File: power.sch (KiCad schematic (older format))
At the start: 157 parts, among them J1 Conn_BAT, Q1 BSS138, Q2 BSS138, Q3 BSS138, Q4 BSS138, Q5 BSS138, SW1 SW_WAKEUP, SW2 SW_RESET, U1 SAMA5D2x-SIP, U3 ACT8945A

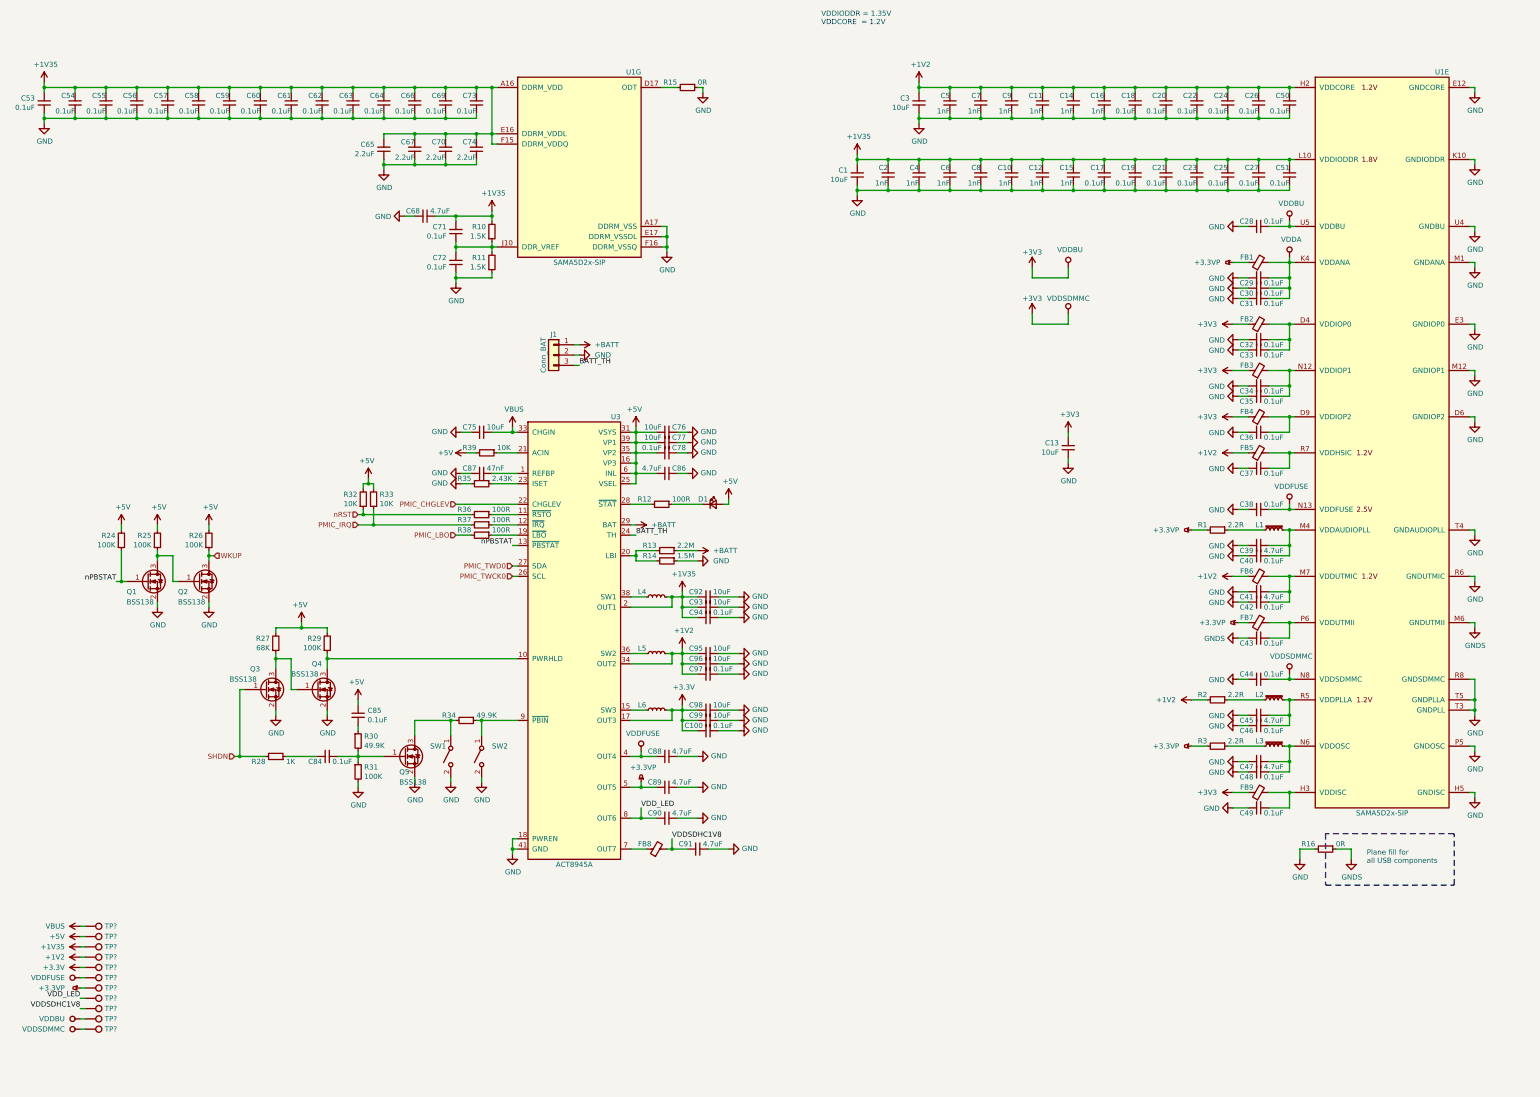
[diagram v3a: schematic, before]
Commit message: Finish schematic (?), set footprints and start placement
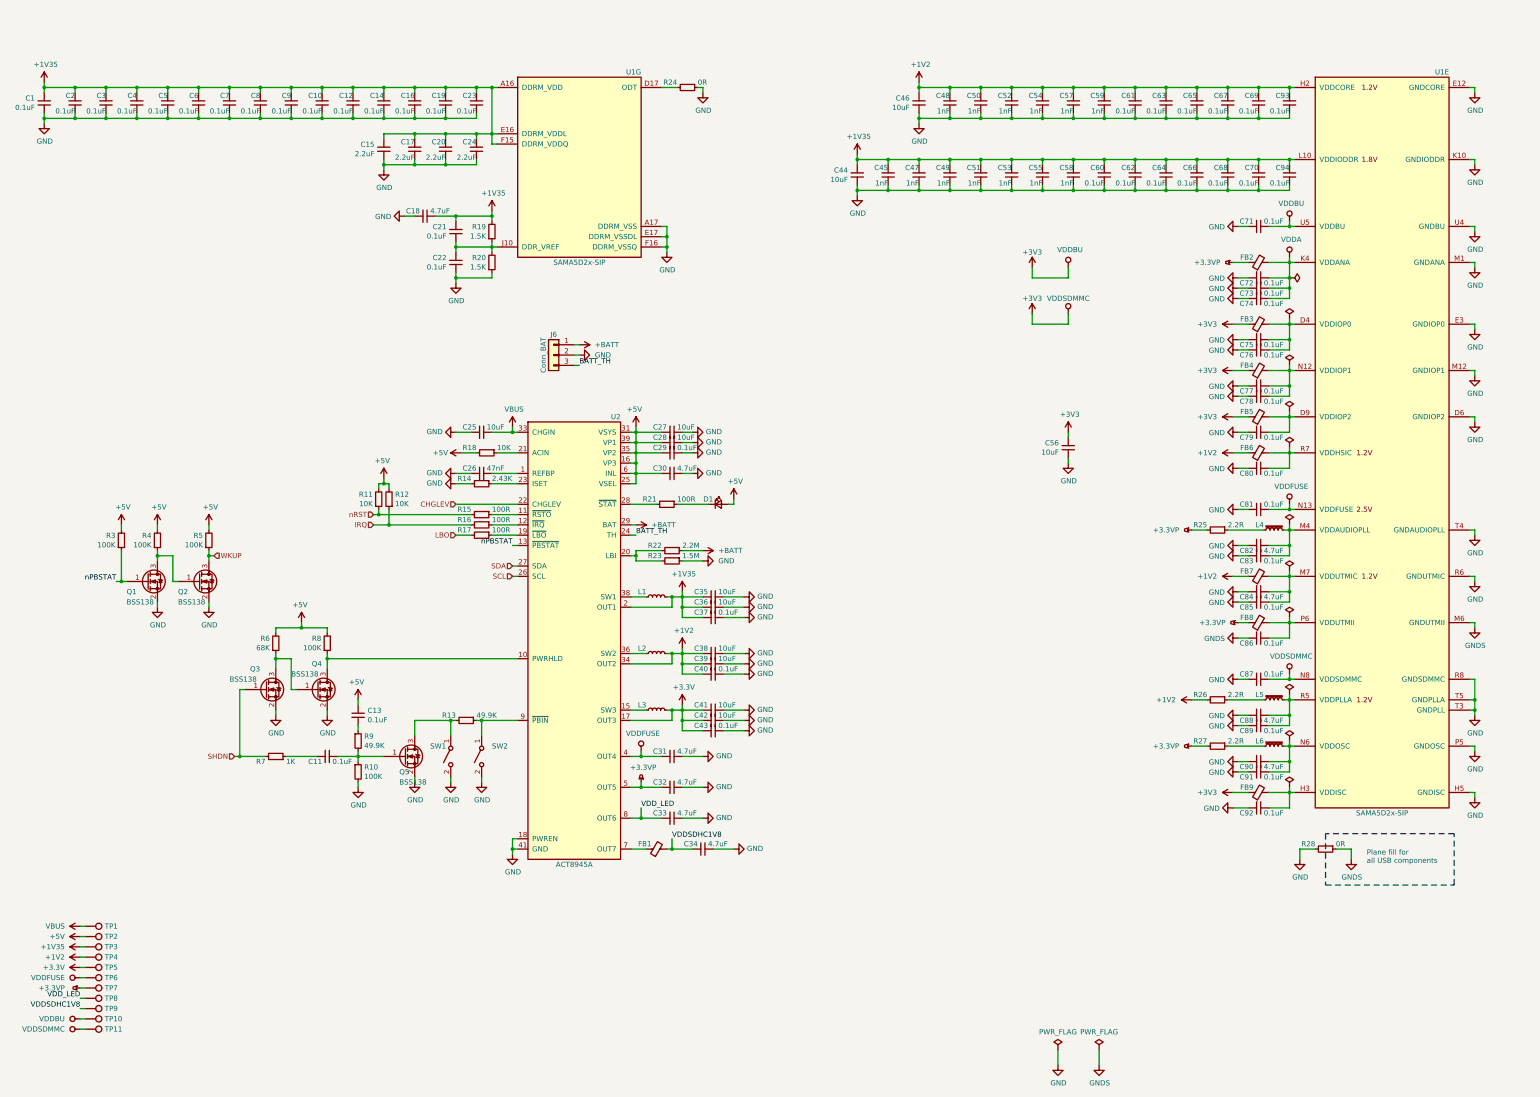
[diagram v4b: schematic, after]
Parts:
- C1: renamed from C53; footprint Capacitor_SMD:C_0603_1608Metric -> Capacitor_SMD:C_0402_1005Metric
- C10: renamed from C62; footprint Capacitor_SMD:C_0603_1608Metric -> Capacitor_SMD:C_0402_1005Metric
- C11: renamed from C84; footprint Capacitor_SMD:C_0603_1608Metric -> Capacitor_SMD:C_0402_1005Metric
- C12: renamed from C63; footprint Capacitor_SMD:C_0603_1608Metric -> Capacitor_SMD:C_0402_1005Metric
- C13: renamed from C85; footprint (none) -> Capacitor_SMD:C_0402_1005Metric
- C14: renamed from C64; footprint Capacitor_SMD:C_0603_1608Metric -> Capacitor_SMD:C_0402_1005Metric
- C15: renamed from C65; footprint Capacitor_SMD:C_0603_1608Metric -> Capacitor_SMD:C_0402_1005Metric
- C16: renamed from C66; footprint Capacitor_SMD:C_0603_1608Metric -> Capacitor_SMD:C_0402_1005Metric
- C17: renamed from C67; footprint Capacitor_SMD:C_0603_1608Metric -> Capacitor_SMD:C_0402_1005Metric
- C18: renamed from C68; footprint Capacitor_SMD:C_0603_1608Metric -> Capacitor_SMD:C_0402_1005Metric
- C19: renamed from C69; footprint Capacitor_SMD:C_0603_1608Metric -> Capacitor_SMD:C_0402_1005Metric
- C2: renamed from C54; footprint Capacitor_SMD:C_0603_1608Metric -> Capacitor_SMD:C_0402_1005Metric
- C20: renamed from C70; footprint Capacitor_SMD:C_0603_1608Metric -> Capacitor_SMD:C_0402_1005Metric
- C21: renamed from C71; footprint (none) -> Capacitor_SMD:C_0402_1005Metric
- C22: renamed from C72; footprint (none) -> Capacitor_SMD:C_0402_1005Metric
- C23: renamed from C73; footprint Capacitor_SMD:C_0603_1608Metric -> Capacitor_SMD:C_0402_1005Metric
- C24: renamed from C74; footprint Capacitor_SMD:C_0603_1608Metric -> Capacitor_SMD:C_0402_1005Metric
- C25: renamed from C75; footprint Capacitor_SMD:C_0603_1608Metric -> Capacitor_SMD:C_0402_1005Metric
- C26: renamed from C87; footprint Capacitor_SMD:C_0603_1608Metric -> Capacitor_SMD:C_0402_1005Metric
- C27: renamed from C76; footprint Capacitor_SMD:C_0603_1608Metric -> Capacitor_SMD:C_0402_1005Metric
- C28: renamed from C77; footprint Capacitor_SMD:C_0603_1608Metric -> Capacitor_SMD:C_0402_1005Metric
- C29: renamed from C78; footprint Capacitor_SMD:C_0603_1608Metric -> Capacitor_SMD:C_0402_1005Metric
- C3: renamed from C55; footprint Capacitor_SMD:C_0603_1608Metric -> Capacitor_SMD:C_0402_1005Metric
- C30: renamed from C86; footprint Capacitor_SMD:C_0603_1608Metric -> Capacitor_SMD:C_0402_1005Metric
- C31: renamed from C88; footprint Capacitor_SMD:C_0603_1608Metric -> Capacitor_SMD:C_0402_1005Metric
- C32: renamed from C89; footprint Capacitor_SMD:C_0603_1608Metric -> Capacitor_SMD:C_0402_1005Metric
- C33: renamed from C90; footprint Capacitor_SMD:C_0603_1608Metric -> Capacitor_SMD:C_0402_1005Metric
- C34: renamed from C91; footprint Capacitor_SMD:C_0603_1608Metric -> Capacitor_SMD:C_0402_1005Metric
- C35: renamed from C92; footprint Capacitor_SMD:C_0603_1608Metric -> Capacitor_SMD:C_0402_1005Metric
- C36: renamed from C93; footprint Capacitor_SMD:C_0603_1608Metric -> Capacitor_SMD:C_0402_1005Metric
- C37: renamed from C94; footprint Capacitor_SMD:C_0603_1608Metric -> Capacitor_SMD:C_0402_1005Metric
- C38: renamed from C95; footprint Capacitor_SMD:C_0603_1608Metric -> Capacitor_SMD:C_0402_1005Metric
- C39: renamed from C96; footprint Capacitor_SMD:C_0603_1608Metric -> Capacitor_SMD:C_0402_1005Metric
- C4: renamed from C56; footprint Capacitor_SMD:C_0603_1608Metric -> Capacitor_SMD:C_0402_1005Metric
- C40: renamed from C97; footprint Capacitor_SMD:C_0603_1608Metric -> Capacitor_SMD:C_0402_1005Metric
- C41: renamed from C98; footprint Capacitor_SMD:C_0603_1608Metric -> Capacitor_SMD:C_0402_1005Metric
- C42: renamed from C99; footprint Capacitor_SMD:C_0603_1608Metric -> Capacitor_SMD:C_0402_1005Metric
- C43: renamed from C100; footprint Capacitor_SMD:C_0603_1608Metric -> Capacitor_SMD:C_0402_1005Metric
- C44: renamed from C1; footprint Capacitor_SMD:C_0603_1608Metric -> Capacitor_SMD:C_0402_1005Metric
- C45: renamed from C2; footprint Capacitor_SMD:C_0603_1608Metric -> Capacitor_SMD:C_0402_1005Metric
- C46: renamed from C3; footprint Capacitor_SMD:C_0603_1608Metric -> Capacitor_SMD:C_0402_1005Metric
- C47: renamed from C4; footprint Capacitor_SMD:C_0603_1608Metric -> Capacitor_SMD:C_0402_1005Metric
- C48: renamed from C5; footprint Capacitor_SMD:C_0603_1608Metric -> Capacitor_SMD:C_0402_1005Metric
- C49: renamed from C6; footprint Capacitor_SMD:C_0603_1608Metric -> Capacitor_SMD:C_0402_1005Metric
- C5: renamed from C57; footprint Capacitor_SMD:C_0603_1608Metric -> Capacitor_SMD:C_0402_1005Metric
- C50: renamed from C7; footprint Capacitor_SMD:C_0603_1608Metric -> Capacitor_SMD:C_0402_1005Metric
- C51: renamed from C8; footprint Capacitor_SMD:C_0603_1608Metric -> Capacitor_SMD:C_0402_1005Metric
- C52: renamed from C9; footprint Capacitor_SMD:C_0603_1608Metric -> Capacitor_SMD:C_0402_1005Metric
- C53: renamed from C10; footprint Capacitor_SMD:C_0603_1608Metric -> Capacitor_SMD:C_0402_1005Metric
- C54: renamed from C11; footprint Capacitor_SMD:C_0603_1608Metric -> Capacitor_SMD:C_0402_1005Metric
- C55: renamed from C12; footprint Capacitor_SMD:C_0603_1608Metric -> Capacitor_SMD:C_0402_1005Metric
- C56: renamed from C13; footprint Capacitor_SMD:C_0603_1608Metric -> Capacitor_SMD:C_0402_1005Metric
- C57: renamed from C14; footprint Capacitor_SMD:C_0603_1608Metric -> Capacitor_SMD:C_0402_1005Metric
- C58: renamed from C15; footprint Capacitor_SMD:C_0603_1608Metric -> Capacitor_SMD:C_0402_1005Metric
- C59: renamed from C16; footprint Capacitor_SMD:C_0603_1608Metric -> Capacitor_SMD:C_0402_1005Metric
- C6: renamed from C58; footprint Capacitor_SMD:C_0603_1608Metric -> Capacitor_SMD:C_0402_1005Metric
- C60: renamed from C17; footprint Capacitor_SMD:C_0603_1608Metric -> Capacitor_SMD:C_0402_1005Metric
- C61: renamed from C18; footprint Capacitor_SMD:C_0603_1608Metric -> Capacitor_SMD:C_0402_1005Metric
- C62: renamed from C19; footprint Capacitor_SMD:C_0603_1608Metric -> Capacitor_SMD:C_0402_1005Metric
- C63: renamed from C20; footprint Capacitor_SMD:C_0603_1608Metric -> Capacitor_SMD:C_0402_1005Metric
- C64: renamed from C21; footprint Capacitor_SMD:C_0603_1608Metric -> Capacitor_SMD:C_0402_1005Metric
- C65: renamed from C22; footprint Capacitor_SMD:C_0603_1608Metric -> Capacitor_SMD:C_0402_1005Metric
- C66: renamed from C23; footprint Capacitor_SMD:C_0603_1608Metric -> Capacitor_SMD:C_0402_1005Metric
- C67: renamed from C24; footprint Capacitor_SMD:C_0603_1608Metric -> Capacitor_SMD:C_0402_1005Metric
- C68: renamed from C25; footprint Capacitor_SMD:C_0603_1608Metric -> Capacitor_SMD:C_0402_1005Metric
- C69: renamed from C26; footprint Capacitor_SMD:C_0603_1608Metric -> Capacitor_SMD:C_0402_1005Metric
- C7: renamed from C59; footprint Capacitor_SMD:C_0603_1608Metric -> Capacitor_SMD:C_0402_1005Metric
- C70: renamed from C27; footprint Capacitor_SMD:C_0603_1608Metric -> Capacitor_SMD:C_0402_1005Metric
- C71: renamed from C28; footprint Capacitor_SMD:C_0603_1608Metric -> Capacitor_SMD:C_0402_1005Metric
- C72: renamed from C29; footprint Capacitor_SMD:C_0603_1608Metric -> Capacitor_SMD:C_0402_1005Metric
- C73: renamed from C30; footprint Capacitor_SMD:C_0603_1608Metric -> Capacitor_SMD:C_0402_1005Metric
- C74: renamed from C31; footprint Capacitor_SMD:C_0603_1608Metric -> Capacitor_SMD:C_0402_1005Metric
- C75: renamed from C32; footprint Capacitor_SMD:C_0603_1608Metric -> Capacitor_SMD:C_0402_1005Metric
- C76: renamed from C33; footprint Capacitor_SMD:C_0603_1608Metric -> Capacitor_SMD:C_0402_1005Metric
- C77: renamed from C34; footprint Capacitor_SMD:C_0603_1608Metric -> Capacitor_SMD:C_0402_1005Metric
- C78: renamed from C35; footprint Capacitor_SMD:C_0603_1608Metric -> Capacitor_SMD:C_0402_1005Metric
- C79: renamed from C36; footprint Capacitor_SMD:C_0603_1608Metric -> Capacitor_SMD:C_0402_1005Metric
- C8: renamed from C60; footprint Capacitor_SMD:C_0603_1608Metric -> Capacitor_SMD:C_0402_1005Metric
- C80: renamed from C37; footprint Capacitor_SMD:C_0603_1608Metric -> Capacitor_SMD:C_0402_1005Metric
- C81: renamed from C38; footprint Capacitor_SMD:C_0603_1608Metric -> Capacitor_SMD:C_0402_1005Metric
- C82: renamed from C39; footprint Capacitor_SMD:C_0603_1608Metric -> Capacitor_SMD:C_0402_1005Metric
- C83: renamed from C40; footprint Capacitor_SMD:C_0603_1608Metric -> Capacitor_SMD:C_0402_1005Metric
- C84: renamed from C41; footprint Capacitor_SMD:C_0603_1608Metric -> Capacitor_SMD:C_0402_1005Metric
- C85: renamed from C42; footprint Capacitor_SMD:C_0603_1608Metric -> Capacitor_SMD:C_0402_1005Metric
- C86: renamed from C43; footprint Capacitor_SMD:C_0603_1608Metric -> Capacitor_SMD:C_0402_1005Metric
- C87: renamed from C44; footprint Capacitor_SMD:C_0603_1608Metric -> Capacitor_SMD:C_0402_1005Metric
- C88: renamed from C45; footprint Capacitor_SMD:C_0603_1608Metric -> Capacitor_SMD:C_0402_1005Metric
- C89: renamed from C46; footprint Capacitor_SMD:C_0603_1608Metric -> Capacitor_SMD:C_0402_1005Metric
- C9: renamed from C61; footprint Capacitor_SMD:C_0603_1608Metric -> Capacitor_SMD:C_0402_1005Metric
- C90: renamed from C47; footprint Capacitor_SMD:C_0603_1608Metric -> Capacitor_SMD:C_0402_1005Metric
- C91: renamed from C48; footprint Capacitor_SMD:C_0603_1608Metric -> Capacitor_SMD:C_0402_1005Metric
- C92: renamed from C49; footprint Capacitor_SMD:C_0603_1608Metric -> Capacitor_SMD:C_0402_1005Metric
- C93: renamed from C50; footprint Capacitor_SMD:C_0603_1608Metric -> Capacitor_SMD:C_0402_1005Metric
- C94: renamed from C51; footprint Capacitor_SMD:C_0603_1608Metric -> Capacitor_SMD:C_0402_1005Metric
- D1: footprint (none) -> LED_SMD:LED_0603_1608Metric
- FB2: renamed from FB1; value BLM03AX100SZ1 -> 10R 1A
- FB3: renamed from FB2; value BLM03AX100SZ1 -> 10R 1A
- FB4: renamed from FB3; value BLM03AX100SZ1 -> 10R 1A
- FB5: renamed from FB4; value BLM03AX100SZ1 -> 10R 1A
- FB6: renamed from FB5; value BLM03AX100SZ1 -> 10R 1A
- FB7: renamed from FB6; value BLM03AX100SZ1 -> 10R 1A
- FB8: renamed from FB7; value BLM03AX100SZ1 -> 10R 1A
- FB9: value BLM03AX100SZ1 -> 10R 1A
- J6: renamed from J1; footprint (none) -> Connector_PinHeader_2.54mm:PinHeader_1x03_P2.54mm_Vertical
- L1: renamed from L4; footprint (none) -> Inductor_SMD:L_Taiyo-Yuden_MD-3030
- L2: renamed from L5; footprint (none) -> Inductor_SMD:L_Taiyo-Yuden_MD-3030
- L3: renamed from L6; footprint (none) -> Inductor_SMD:L_Taiyo-Yuden_MD-3030
- R10: renamed from R31; footprint (none) -> Resistor_SMD:R_0603_1608Metric
- R11: renamed from R32; footprint (none) -> Resistor_SMD:R_0603_1608Metric
- R12: renamed from R33; footprint (none) -> Resistor_SMD:R_0603_1608Metric
- R13: renamed from R34; footprint (none) -> Resistor_SMD:R_0603_1608Metric
- R14: renamed from R35; footprint (none) -> Resistor_SMD:R_0603_1608Metric
- R15: renamed from R36; footprint (none) -> Resistor_SMD:R_0603_1608Metric
- R16: renamed from R37; footprint (none) -> Resistor_SMD:R_0603_1608Metric
- R17: renamed from R38; footprint (none) -> Resistor_SMD:R_0603_1608Metric
- R18: renamed from R39; footprint (none) -> Resistor_SMD:R_0603_1608Metric
- R19: renamed from R10; footprint (none) -> Resistor_SMD:R_0603_1608Metric
- R20: renamed from R11; footprint (none) -> Resistor_SMD:R_0603_1608Metric
- R21: renamed from R12; footprint (none) -> Resistor_SMD:R_0603_1608Metric
- R22: renamed from R13; footprint (none) -> Resistor_SMD:R_0603_1608Metric
- R23: renamed from R14; footprint (none) -> Resistor_SMD:R_0603_1608Metric
- R24: renamed from R15; footprint (none) -> Resistor_SMD:R_0603_1608Metric
- R3: renamed from R24; footprint (none) -> Resistor_SMD:R_0603_1608Metric
- R4: renamed from R25; footprint (none) -> Resistor_SMD:R_0603_1608Metric
- R5: renamed from R26; footprint (none) -> Resistor_SMD:R_0603_1608Metric
- R6: renamed from R27; footprint (none) -> Resistor_SMD:R_0603_1608Metric
- R7: renamed from R28; footprint (none) -> Resistor_SMD:R_0603_1608Metric
- R8: renamed from R29; footprint (none) -> Resistor_SMD:R_0603_1608Metric
- R9: renamed from R30; footprint (none) -> Resistor_SMD:R_0603_1608Metric
- SW1, SW2: footprint (none) -> Button_Switch_SMD:SW_SPST_FSMSM
- TP1, TP10, TP11, TP2, TP3, TP4, TP5, TP6, TP7, TP8, TP9: renamed from TP?; footprint (none) -> TestPoint:TestPoint_Pad_D1.5mm
- U2: renamed from U3; footprint (none) -> Package_DFN_QFN:QFN-40-1EP_5x5mm_P0.4mm_EP3.6x3.6mm
- renumbered FB8 to FB1, L1 to L4, L2 to L5, L3 to L6, R1 to R25, R2 to R26, R3 to R27, R16 to R28
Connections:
- net +5V: now also C27.2, C28.2, C29.2, C30.2; no longer C27.1, C28.1, C29.1, C30.1
- net GND: now also C27.1, C28.1, C29.1, C30.1; no longer C27.2, C28.2, C29.2, C30.2
- net PMIC_CHGLEV renamed CHGLEV
- net PMIC_IRQ renamed IRQ
- net PMIC_LBO renamed LBO
- net PMIC_TWCK0 renamed SCL
- net PMIC_TWD0 renamed SDA
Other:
- note removed: "VDDIODDR = 1.35V\nVDDCORE = 1.2V"
- moved on the sheet: C27, C28, C29, C30, C31, C32, C33, C34, C35, C36, C37, C38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

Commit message: More routing, 165 unconnected left
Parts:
- FB2, FB3, FB4, FB5, FB6, FB7, FB8, FB9: value 10R 1A -> BLM18PG300SN1D
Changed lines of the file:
@@
 P 13050 4600
 F 0 "FB5" V 13100 4650 50  0000 L CNN
-F 1 "10R 1A" V 13196 4600 50  0001 C CNN
+F 1 "BLM18PG300SN1D" V 13196 4600 50  0001 C CNN
 F 2 "Inductor_SMD:L_0603_1608Metric" V 12980 4600 50  0001 C CNN
 F 3 "~" H 13050 4600 50  0001 C CNN
@@
 P 13050 4150
 F 0 "FB4" V 13100 4200 50  0000 L CNN
-F 1 "10R 1A" V 13196 4150 50  0001 C CNN
+F 1 "BLM18PG300SN1D" V 13196 4150 50  0001 C CNN
 F 2 "Inductor_SMD:L_0603_1608Metric" V 12980 4150 50  0001 C CNN
 F 3 "~" H 13050 4150 50  0001 C CNN
@@
 P 13050 3700
 F 0 "FB3" V 13100 3750 50  0000 L CNN
-F 1 "10R 1A" V 13196 3700 50  0001 C CNN
+F 1 "BLM18PG300SN1D" V 13196 3700 50  0001 C CNN
 F 2 "Inductor_SMD:L_0603_1608Metric" V 12980 3700 50  0001 C CNN
 F 3 "~" H 13050 3700 50  0001 C CNN
@@
 P 13050 6600
 F 0 "FB8" V 13100 6650 50  0000 L CNN
-F 1 "10R 1A" V 13196 6600 50  0001 C CNN
+F 1 "BLM18PG300SN1D" V 13196 6600 50  0001 C CNN
 F 2 "Inductor_SMD:L_0603_1608Metric" V 12980 6600 50  0001 C CNN
 F 3 "~" H 13050 6600 50  0001 C CNN
@@
 P 13050 3100
 F 0 "FB2" V 13100 3150 50  0000 L CNN
-F 1 "10R 1A" V 13196 3100 50  0001 C CNN
+F 1 "BLM18PG300SN1D" V 13196 3100 50  0001 C CNN
 F 2 "Inductor_SMD:L_0603_1608Metric" V 12980 3100 50  0001 C CNN
 F 3 "~" H 13050 3100 50  0001 C CNN
@@
 P 13050 4950
 F 0 "FB6" V 13100 5000 50  0000 L CNN
-F 1 "10R 1A" V 13196 4950 50  0001 C CNN
+F 1 "BLM18PG300SN1D" V 13196 4950 50  0001 C CNN
 F 2 "Inductor_SMD:L_0603_1608Metric" V 12980 4950 50  0001 C CNN
 F 3 "~" H 13050 4950 50  0001 C CNN
@@
 P 13050 6150
 F 0 "FB7" V 13100 6200 50  0000 L CNN
-F 1 "10R 1A" V 13196 6150 50  0001 C CNN
+F 1 "BLM18PG300SN1D" V 13196 6150 50  0001 C CNN
 F 2 "Inductor_SMD:L_0603_1608Metric" V 12980 6150 50  0001 C CNN
 F 3 "~" H 13050 6150 50  0001 C CNN
@@
 P 13050 8250
 F 0 "FB9" V 13100 8300 50  0000 L CNN
-F 1 "10R 1A" V 13196 8250 50  0001 C CNN
+F 1 "BLM18PG300SN1D" V 13196 8250 50  0001 C CNN
 F 2 "Inductor_SMD:L_0603_1608Metric" V 12980 8250 50  0001 C CNN
 F 3 "~" H 13050 8250 50  0001 C CNN

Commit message: Almost routed, just 2 unconnected left
Hahahahahah HahahaHhahaHAHAhahahHAHAHAHhahah
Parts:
- removed TP10: TP_VDDBU, TestPoint:TestPoint_Pad_D1.5mm, symbol Connector:TestPoint
- removed TP5: TP_3.3V, TestPoint:TestPoint_Pad_D1.5mm, symbol Connector:TestPoint
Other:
- moved on the sheet: TP11, TP6, TP7, TP8, TP9
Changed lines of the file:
@@
 L power:+3.3V #PWR018
 U 1 1 5D2824FD
+P 1600 10350
+F 0 "#PWR018" H 1600 10200 50  0001 C CNN
+F 1 "+3.3V" V 1600 10500 50  0000 L CNN
+F 2 "" H 1600 10350 50  0001 C CNN
+F 3 "" H 1600 10350 50  0001 C CNN
+	1    1600 10350
+	0    -1   -1   0
+$EndComp
+$Comp
+L power_extra:VDDFUSE #PWR019
+U 1 1 5D282CAD
 P 1600 9950
-F 0 "#PWR018" H 1600 9800 50  0001 C CNN
-F 1 "+3.3V" V 1600 10100 50  0000 L CNN
+F 0 "#PWR019" H 1600 9800 50  0001 C CNN
+F 1 "VDDFUSE" V 1600 10100 50  0000 L CNN
 F 2 "" H 1600 9950 50  0001 C CNN
 F 3 "" H 1600 9950 50  0001 C CNN
@@
 $EndComp
 $Comp
-L power_extra:VDDFUSE #PWR019
-U 1 1 5D282CAD
+L power:+3.3VP #PWR020
+U 1 1 5D283274
 P 1600 10050
-F 0 "#PWR019" H 1600 9900 50  0001 C CNN
-F 1 "VDDFUSE" V 1600 10200 50  0000 L CNN
+F 0 "#PWR020" H 1750 10000 50  0001 C CNN
+F 1 "+3.3VP" V 1600 10200 50  0000 L CNN
 F 2 "" H 1600 10050 50  0001 C CNN
 F 3 "" H 1600 10050 50  0001 C CNN
@@
 	0    -1   -1   0
 $EndComp
-$Comp
-L power:+3.3VP #PWR020
-U 1 1 5D283274
-P 1600 10150
-F 0 "#PWR020" H 1750 10100 50  0001 C CNN
-F 1 "+3.3VP" V 1600 10300 50  0000 L CNN
-F 2 "" H 1600 10150 50  0001 C CNN
-F 3 "" H 1600 10150 50  0001 C CNN
-	1    1600 10150
-	0    -1   -1   0
-$EndComp
+Text Label 1600 10150 2    50   ~ 0
+VDD_LED
 Text Label 1600 10250 2    50   ~ 0
-VDD_LED
-Text Label 1600 10350 2    50   ~ 0
 VDDSDHC1V8
-$Comp
-L power_extra:VDDBU #PWR021
-U 1 1 5D284AD4
-P 1600 10450
-F 0 "#PWR021" H 1600 10300 50  0001 C CNN
-F 1 "VDDBU" V 1600 10600 50  0000 L CNN
-F 2 "" H 1600 10450 50  0001 C CNN
-F 3 "" H 1600 10450 50  0001 C CNN
-	1    1600 10450
-	0    -1   -1   0
-$EndComp
-$Comp
-L power_extra:VDDSDMMC #PWR022
-U 1 1 5D285143
-P 1600 10550
-F 0 "#PWR022" H 1600 10400 50  0001 C CNN
-F 1 "VDDSDMMC" V 1600 10700 50  0000 L CNN
-F 2 "" H 1600 10550 50  0001 C CNN
-F 3 "" H 1600 10550 50  0001 C CNN
-	1    1600 10550
-	0    -1   -1   0
-$EndComp
 Wire Wire Line
 	1600 9550 1650 9550
@@
 Wire Wire Line
 	1600 10350 1650 10350
-Wire Wire Line
-	1600 10450 1650 10450
-Wire Wire Line
-	1600 10550 1650 10550
 $Comp
 L Connector:TestPoint TP1
@@
 $EndComp
 $Comp
-L Connector:TestPoint TP5
-U 1 1 5D2E9FBE
+L Connector:TestPoint TP6
+U 1 1 5D2EA002
 P 1650 9950
-F 0 "TP5" V 1650 10138 50  0000 L CNN
-F 1 "TP_3.3V" V 1695 10138 50  0001 L CNN
+F 0 "TP6" V 1650 10138 50  0000 L CNN
+F 1 "TP_VDDFUSE" V 1695 10138 50  0001 L CNN
 F 2 "TestPoint:TestPoint_Pad_D1.5mm" H 1850 9950 50  0001 C CNN
 F 3 "~" H 1850 9950 50  0001 C CNN
@@
 $EndComp
 $Comp
-L Connector:TestPoint TP6
-U 1 1 5D2EA002
+L Connector:TestPoint TP7
+U 1 1 5D2EA046
 P 1650 10050
-F 0 "TP6" V 1650 10238 50  0000 L CNN
-F 1 "TP_VDDFUSE" V 1695 10238 50  0001 L CNN
+F 0 "TP7" V 1650 10238 50  0000 L CNN
+F 1 "TP_3.3VP" V 1695 10238 50  0001 L CNN
 F 2 "TestPoint:TestPoint_Pad_D1.5mm" H 1850 10050 50  0001 C CNN
 F 3 "~" H 1850 10050 50  0001 C CNN
@@
 $EndComp
 $Comp
-L Connector:TestPoint TP7
-U 1 1 5D2EA046
+L Connector:TestPoint TP8
+U 1 1 5D2EA0A7
 P 1650 10150
-F 0 "TP7" V 1650 10338 50  0000 L CNN
-F 1 "TP_3.3VP" V 1695 10338 50  0001 L CNN
+F 0 "TP8" V 1650 10338 50  0000 L CNN
+F 1 "TP_VDD_LED" V 1695 10338 50  0001 L CNN
 F 2 "TestPoint:TestPoint_Pad_D1.5mm" H 1850 10150 50  0001 C CNN
 F 3 "~" H 1850 10150 50  0001 C CNN
@@
 $EndComp
 $Comp
-L Connector:TestPoint TP8
-U 1 1 5D2EA0A7
+L Connector:TestPoint TP9
+U 1 1 5D2EA141
 P 1650 10250
-F 0 "TP8" V 1650 10438 50  0000 L CNN
-F 1 "TP_VDD_LED" V 1695 10438 50  0001 L CNN
+F 0 "TP9" V 1650 10438 50  0000 L CNN
+F 1 "TP_VDDSDHC1V8" V 1695 10438 50  0001 L CNN
 F 2 "TestPoint:TestPoint_Pad_D1.5mm" H 1850 10250 50  0001 C CNN
 F 3 "~" H 1850 10250 50  0001 C CNN
@@
 $EndComp
 $Comp
-L Connector:TestPoint TP9
-U 1 1 5D2EA141
+L Connector:TestPoint TP11
+U 1 1 5D2EA26B
 P 1650 10350
-F 0 "TP9" V 1650 10538 50  0000 L CNN
-F 1 "TP_VDDSDHC1V8" V 1695 10538 50  0001 L CNN
+F 0 "TP11" V 1650 10538 50  0000 L CNN
+F 1 "TP_VDDSDMMC" V 1695 10538 50  0001 L CNN
 F 2 "TestPoint:TestPoint_Pad_D1.5mm" H 1850 10350 50  0001 C CNN
 F 3 "~" H 1850 10350 50  0001 C CNN
@@
 	0    1    1    0
 $EndComp
-$Comp
-L Connector:TestPoint TP10
-U 1 1 5D2EA185
-P 1650 10450
-F 0 "TP10" V 1650 10638 50  0000 L CNN
-F 1 "TP_VDDBU" V 1695 10638 50  0001 L CNN
-F 2 "TestPoint:TestPoint_Pad_D1.5mm" H 1850 10450 50  0001 C CNN
-F 3 "~" H 1850 10450 50  0001 C CNN
-	1    1650 10450
-	0    1    1    0
-$EndComp
-$Comp
-L Connector:TestPoint TP11
-U 1 1 5D2EA26B
-P 1650 10550
-F 0 "TP11" V 1650 10738 50  0000 L CNN
-F 1 "TP_VDDSDMMC" V 1695 10738 50  0001 L CNN
-F 2 "TestPoint:TestPoint_Pad_D1.5mm" H 1850 10550 50  0001 C CNN
-F 3 "~" H 1850 10550 50  0001 C CNN
-	1    1650 10550
-	0    1    1    0
-$EndComp
